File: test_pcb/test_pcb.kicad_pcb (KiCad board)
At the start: 2 copper layers, 62.2 x 43.2 mm, 19 parts, among them K0 KEYSW, K1 KEYSW, K2 KEYSW, K3 KEYSW, K5 KEYSW, U1 74HC595, U2 Teensy3.2

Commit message: updated test_pcb
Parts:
- added LVC9_HOLES: LVC9 Attach, cherry_rgb:LVC9_HOLES, F.Cu at (200.0, 94.0)
- added P1: CONN_01X08, Pin_Headers:Pin_Header_Straight_1x08_Pitch2.00mm, F.Cu at (230.0, 78.5)
- added P2: CONN_01X08, Pin_Headers:Pin_Header_Straight_1x08_Pitch2.00mm, F.Cu at (170.0, 92.5)
- added U0: Teensy3.2, Teensy:Teensy30_31_32_LC, F.Cu at (248.0, 90.5)
- U1: footprint SMD_Packages:SO-16-L -> Housings_SSOP:TSSOP-16_4.4x5mm_Pitch0.65mm
- U2: value Teensy3.2 -> 74HC595; footprint Socket_Strips:Socket_Strip_Angled_2x27_Pitch2.54mm -> Housings_SSOP:TSSOP-16_4.4x5mm_Pitch0.65mm; moved to B.Cu
- moved U2 36.3 mm to (223.5, 89.0), turned to 0 degrees
- moved R1 10.6 mm to (215.0, 88.5)
- moved R2 10.6 mm to (224.5, 107.5)
- moved U1 5.64 mm to (223.5, 81.5), turned to 0 degrees
- moved D1 2.07 mm to (174.5, 98.0)
- moved D3 2.03 mm to (193.5, 98.0)
- moved D0 2.02 mm to (184.0, 79.0)
- moved D5 1.99 mm to (212.5, 98.0)
- moved D2 1.98 mm to (203.0, 79.0)
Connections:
- D3 pad 1: Net-(D3-Pad1) -> row1
- U1 pad 1: row1_sled_g -> col0_sled_cath
- U1 pad 11: Net-(U1-Pad11) -> sr_clk0
- U1 pad 13: Net-(U1-Pad13) -> GND
- U1 pad 14: sr_data -> sr_data0
- U1 pad 15: row1_sled_b -> col1_sled_cath
- U1 pad 2: row1_sled_r -> col2_sled_cath
- U1 pad 3: row0_sled_b -> Net-(U1-Pad3)
- U1 pad 4: row0_sled_g -> Net-(U1-Pad4)
- U1 pad 5: row0_sled_r -> Net-(U1-Pad5)
- U1 pad 6: col1_sled_cath -> Net-(U1-Pad6)
- U1 pad 7: col0_sled_cath -> Net-(U1-Pad7)
- U2 pad 1: Net-(U2-Pad1) -> row1_sled_g
- U2 pad 11: Net-(U2-Pad11) -> sr_clk0
- U2 pad 13: Net-(U2-Pad13) -> GND
- U2 pad 14: Net-(U2-Pad14) -> sr_data1
- U2 pad 15: Net-(U2-Pad15) -> row1_sled_b
- U2 pad 16: Net-(U2-Pad16) -> VCC
- U2 pad 2: row0 -> row1_sled_r
- U2 pad 3: row1 -> row0_sled_b
- U2 pad 4: col0 -> row0_sled_g
- U2 pad 5: col1 -> row0_sled_r
- U2 pad 6: sr_data -> Net-(U2-Pad6)
- U2 pad 7: col2_sled_cath -> Net-(U2-Pad7)
- U2 pad 8: Net-(U2-Pad8) -> GND

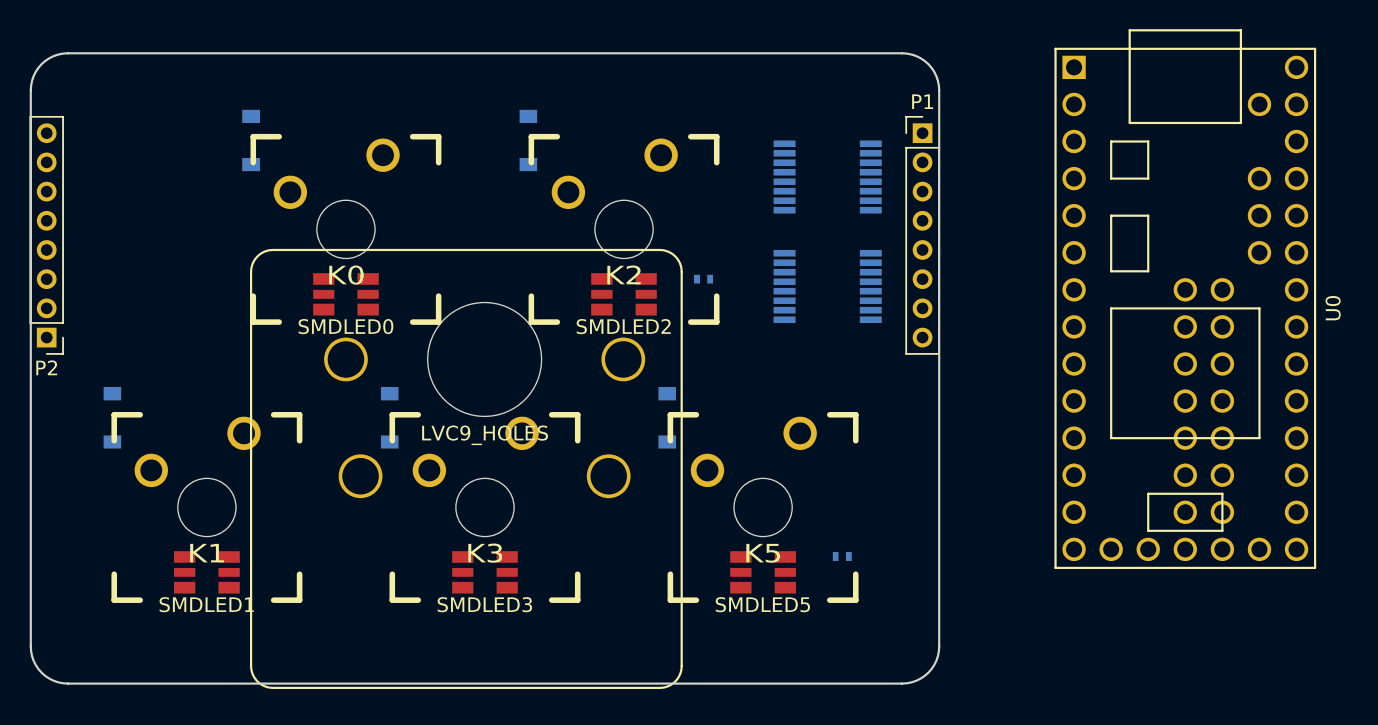
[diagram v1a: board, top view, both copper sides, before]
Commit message: test_pcb first pass complete
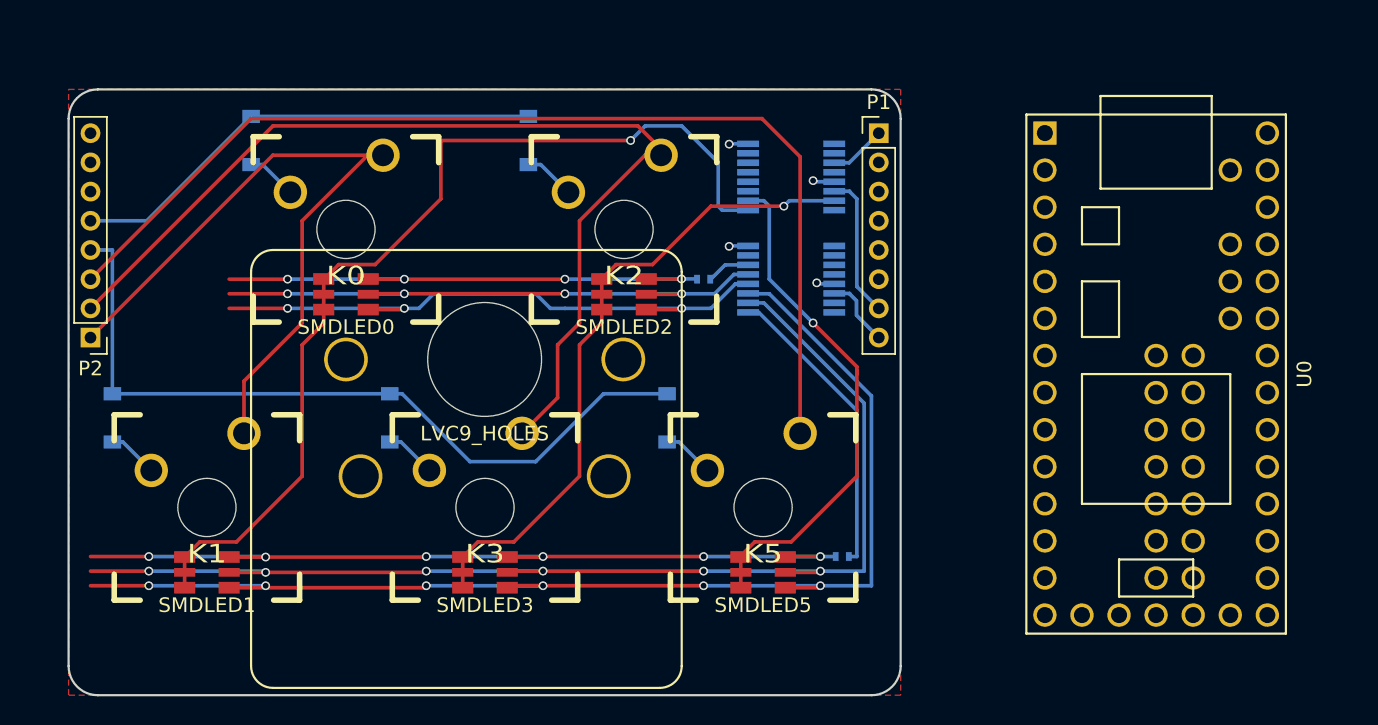
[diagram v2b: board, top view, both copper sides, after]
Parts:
- moved U0 4.92 mm to (246.0, 95.0)
- moved P1 3.00 mm to (227.0, 78.5)
- moved P2 3.00 mm to (173.0, 92.5)
- moved U2 2.55 mm to (221.0, 88.5)
- moved U1 2.50 mm to (221.0, 81.5)
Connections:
- U2 pad 1: row1_sled_g -> row1_sled_r
- U2 pad 15: row1_sled_b -> Net-(U2-Pad15)
- U2 pad 2: row1_sled_r -> row1_sled_g
- U2 pad 3: row0_sled_b -> row1_sled_b
- U2 pad 4: row0_sled_g -> row0_sled_b
- U2 pad 5: row0_sled_r -> row0_sled_g
- U2 pad 6: Net-(U2-Pad6) -> row0_sled_r
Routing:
- net row1_sled_b: track 0.00 -> 85.5 mm, vias 0 -> 6
- net row1_sled_g: track 0.00 -> 82.8 mm, vias 0 -> 6
- net col2: track 0.00 -> 73.2 mm
- net col1: track 0.00 -> 69.0 mm, vias 0 -> 1
- net col0_sled_cath: track 0.00 -> 66.5 mm, vias 0 -> 1
- net Net-(R2-Pad2): track 0.00 -> 58.5 mm, vias 0 -> 6
- net row1: track 0.00 -> 53.2 mm
- net col0: track 0.00 -> 48.8 mm
- net col1_sled_cath: track 0.00 -> 45.0 mm, vias 0 -> 1
- net row0_sled_b: track 0.00 -> 42.0 mm, vias 0 -> 3
- net row0_sled_g: track 0.00 -> 41.0 mm, vias 0 -> 4
- net Net-(R1-Pad2): track 0.00 -> 37.0 mm, vias 0 -> 4
- net col2_sled_cath: track 0.00 -> 35.2 mm, vias 0 -> 1
- net row0: track 0.00 -> 33.0 mm
- net row1_sled_r: track 0.00 -> 20.8 mm
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- added copper zone on F.Cu, net GND
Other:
- board size 62.2 x 43.2 mm -> 57 x 41.5 mm

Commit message: test_pcb small stuff
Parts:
- added P0: CONN_01X08, Connectors_Molex:Molex_PicoBlade_53261-0871_08x1.25mm_Angled, F.Cu at (197.8, 124.5)
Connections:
- P1 pad 5: Net-(P1-Pad5) -> VCC
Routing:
- net VCC: track 0.00 -> 13.1 mm, vias 0 -> 2

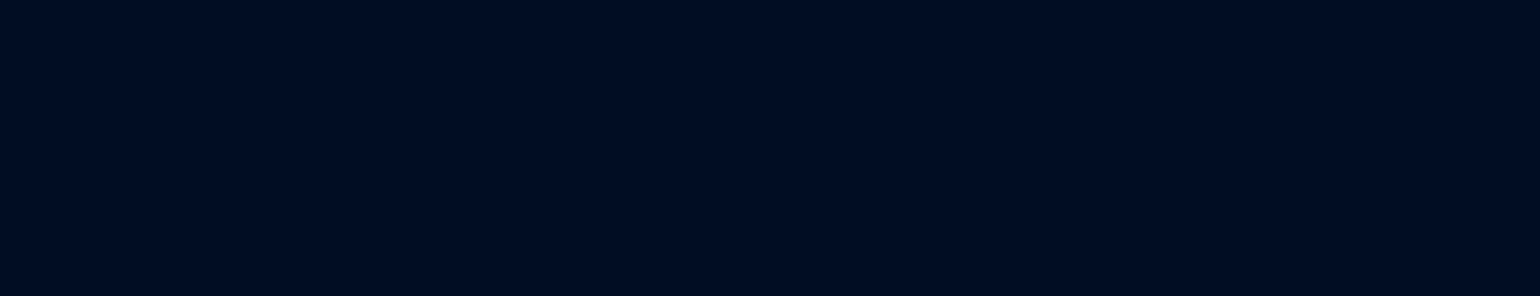
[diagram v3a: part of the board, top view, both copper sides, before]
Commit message: test experiment with 11/12ths keys
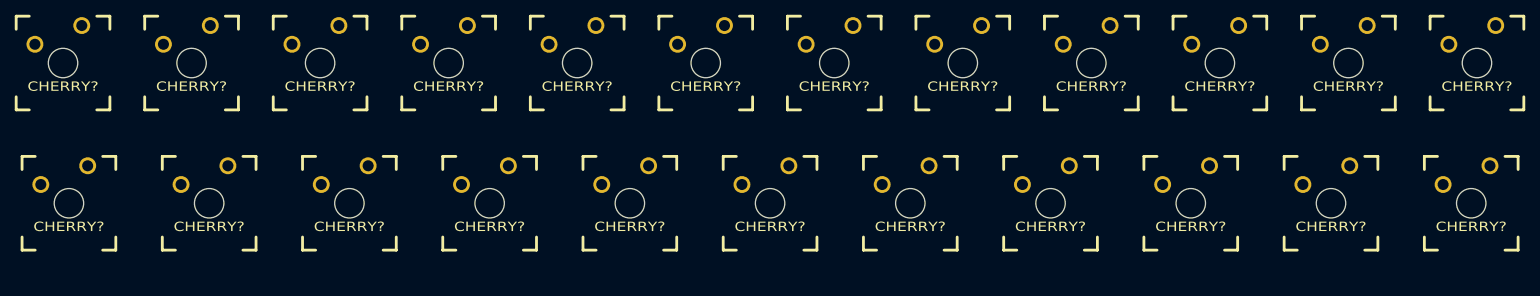
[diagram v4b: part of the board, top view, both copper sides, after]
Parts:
- added CHERRY?: MX, cherry_rgb:CHERRY_PLATE_91.6H, F.Cu at (250.8, 23.0)
- added CHERRY?: MX, cherry_rgb:CHERRY_PLATE_91.6H, F.Cu at (94.0, 23.0)
- added CHERRY?: MX, cherry_rgb:CHERRY_PLATE_91.6H, F.Cu at (76.6, 23.0)
- added CHERRY?: MX, cherry_rgb:CHERRY_PLATE_NH_100H, F.Cu at (250.0, 42.0)
- added CHERRY?: MX, cherry_rgb:CHERRY_PLATE_NH_100H, F.Cu at (60.0, 42.0)
- added CHERRY?: MX, cherry_rgb:CHERRY_PLATE_NH_100H, F.Cu at (231.0, 42.0)
- added CHERRY?: MX, cherry_rgb:CHERRY_PLATE_NH_100H, F.Cu at (79.0, 42.0)
- added CHERRY?: MX, cherry_rgb:CHERRY_PLATE_NH_100H, F.Cu at (98.0, 42.0)
- added CHERRY?: MX, cherry_rgb:CHERRY_PLATE_NH_100H, F.Cu at (212.0, 42.0)
- added CHERRY?: MX, cherry_rgb:CHERRY_PLATE_NH_100H, F.Cu at (193.0, 42.0)
- added CHERRY?: MX, cherry_rgb:CHERRY_PLATE_NH_100H, F.Cu at (174.0, 42.0)
- added CHERRY?: MX, cherry_rgb:CHERRY_PLATE_91.6H, F.Cu at (233.4, 23.0)
- added CHERRY?: MX, cherry_rgb:CHERRY_PLATE_NH_100H, F.Cu at (155.0, 42.0)
- added CHERRY?: MX, cherry_rgb:CHERRY_PLATE_NH_100H, F.Cu at (136.0, 42.0)
- added CHERRY?: MX, cherry_rgb:CHERRY_PLATE_NH_100H, F.Cu at (117.0, 42.0)
- added CHERRY?: MX, cherry_rgb:CHERRY_PLATE_91.6H, F.Cu at (59.2, 23.0)
- added CHERRY?: MX, cherry_rgb:CHERRY_PLATE_91.6H, F.Cu at (215.9, 23.0)
- added CHERRY?: MX, cherry_rgb:CHERRY_PLATE_91.6H, F.Cu at (198.5, 23.0)
- added CHERRY?: MX, cherry_rgb:CHERRY_PLATE_91.6H, F.Cu at (181.1, 23.0)
- added CHERRY?: MX, cherry_rgb:CHERRY_PLATE_91.6H, F.Cu at (163.7, 23.0)
- added CHERRY?: MX, cherry_rgb:CHERRY_PLATE_91.6H, F.Cu at (146.3, 23.0)
- added CHERRY?: MX, cherry_rgb:CHERRY_PLATE_91.6H, F.Cu at (128.9, 23.0)
- added CHERRY?: MX, cherry_rgb:CHERRY_PLATE_91.6H, F.Cu at (111.4, 23.0)

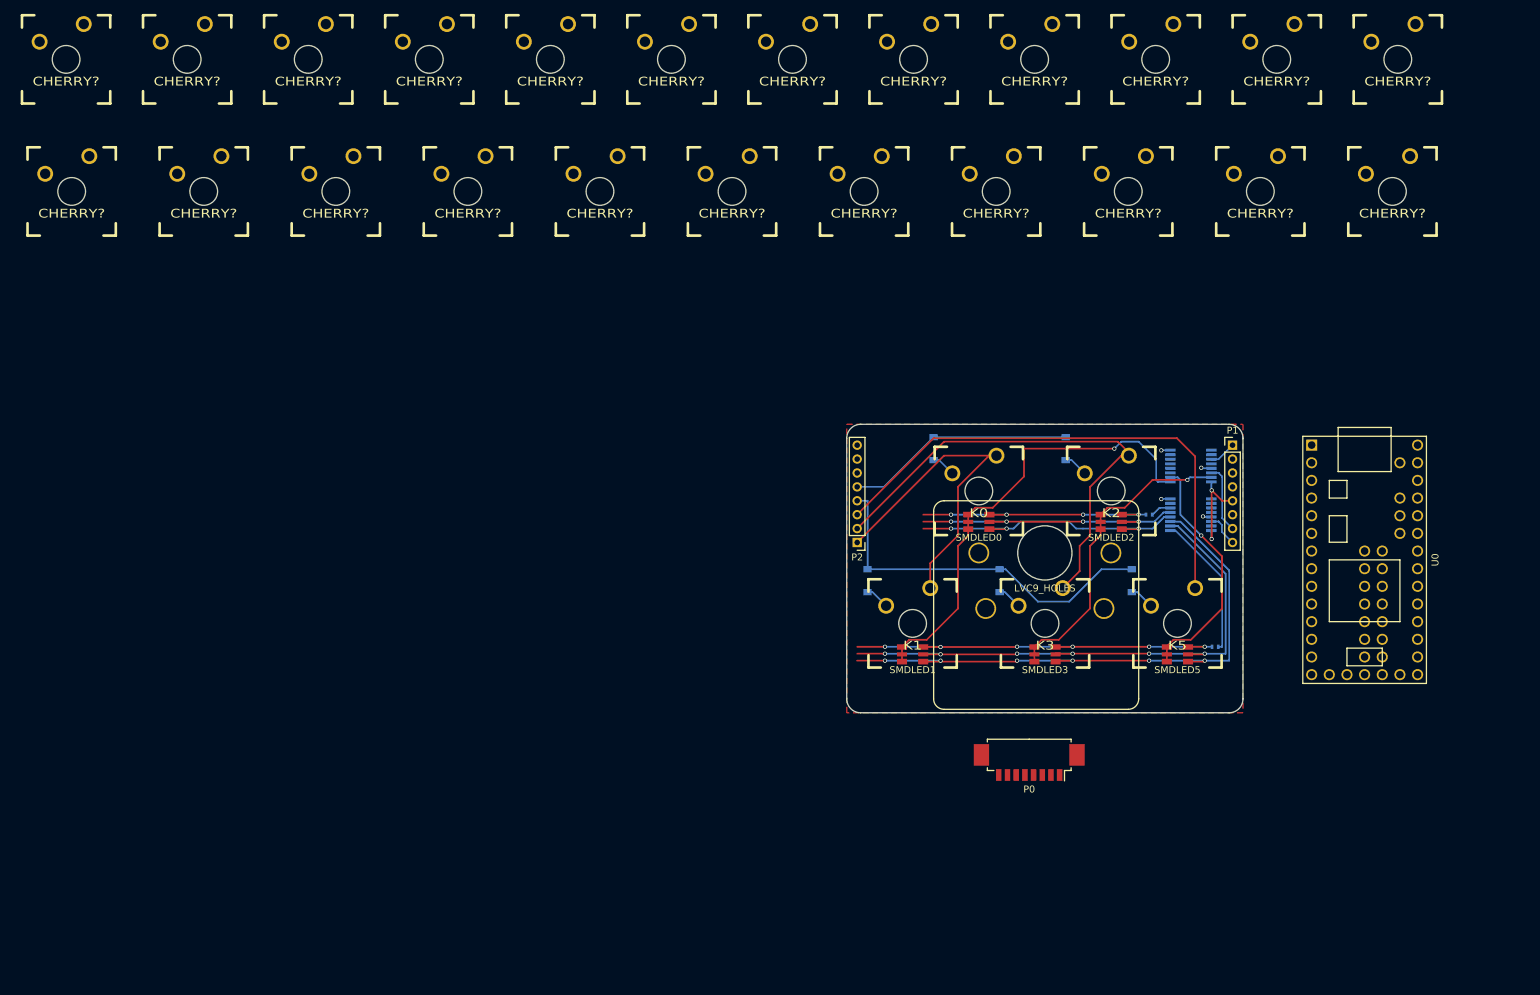
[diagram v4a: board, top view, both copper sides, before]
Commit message: test is now a numpad for led testing + a 6 key test for the trackpoint
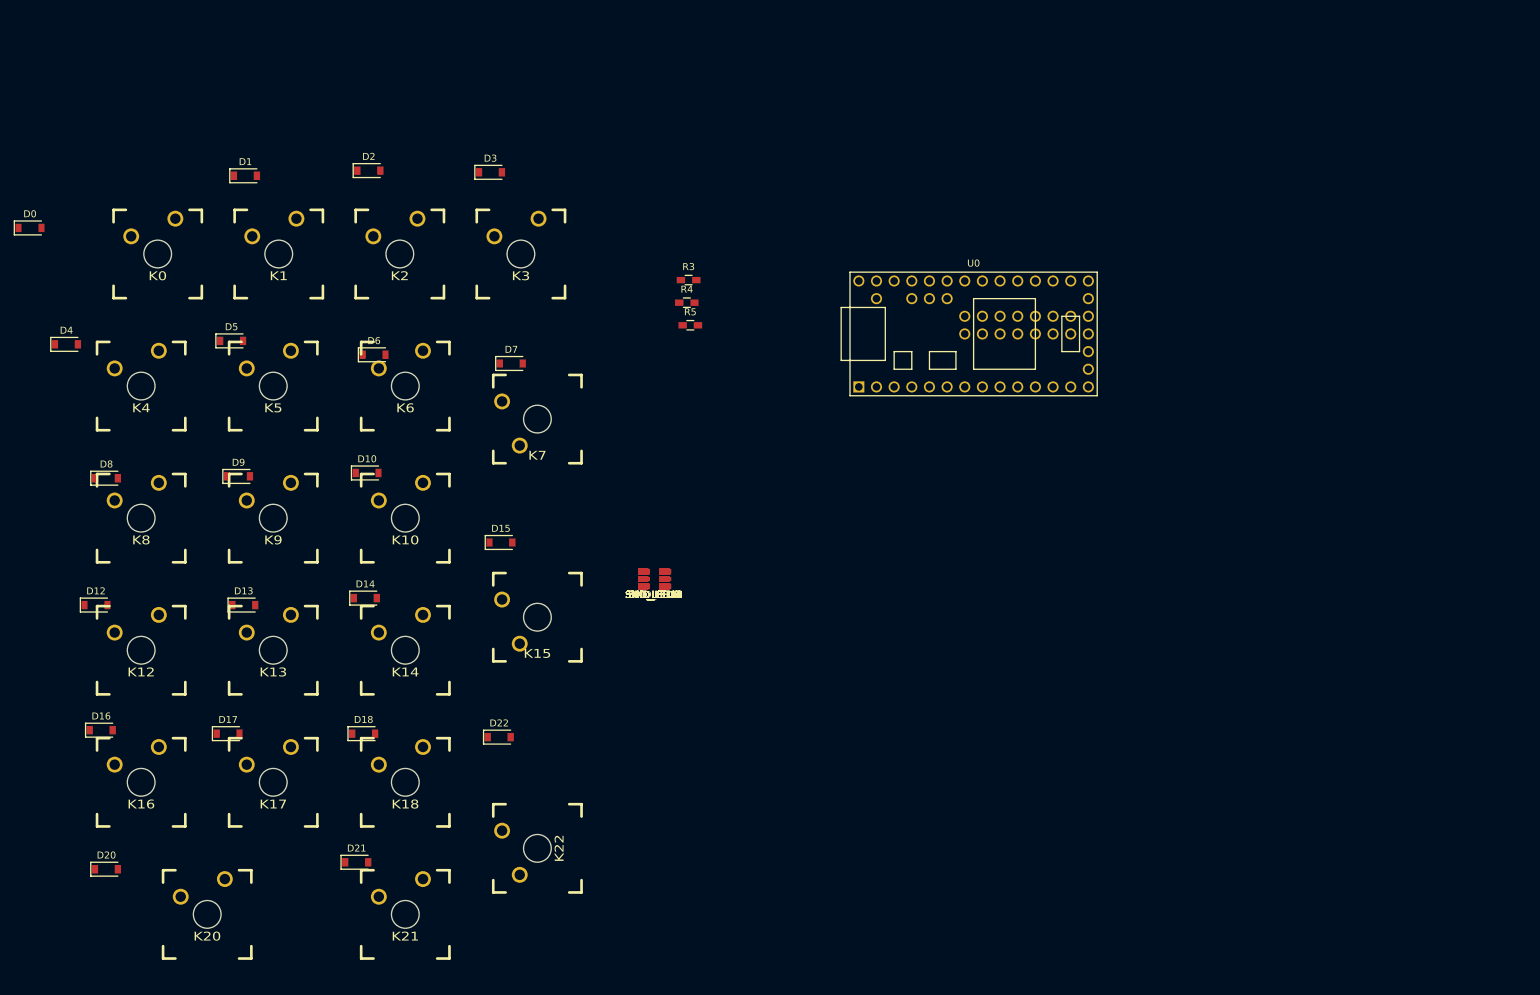
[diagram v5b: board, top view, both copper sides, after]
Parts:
- removed CHERRY? (x12): MX, cherry_rgb:CHERRY_PLATE_91.6H
- removed CHERRY? (x11): MX, cherry_rgb:CHERRY_PLATE_NH_100H
- removed LVC9_HOLES: LVC9 Attach, cherry_rgb:LVC9_HOLES
- removed P0: CONN_01X08, Connectors_Molex:Molex_PicoBlade_53261-0871_08x1.25mm_Angled
- removed P1, P2: CONN_01X08, Pin_Headers:Pin_Header_Straight_1x08_Pitch2.00mm
- removed R1, R2: R, Resistors_SMD:R_0402
- removed SMDLED0, SMDLED1, SMDLED2, SMDLED3, SMDLED5: LED_RGB, cherry_rgb:SMLVN6RGB
- removed U1, U2: 74HC595, Housings_SSOP:TSSOP-16_4.4x5mm_Pitch0.65mm
- added D10: D, Diodes_SMD:D_SOD-123, F.Cu at (102.5, 82.5)
- added D12: D, Diodes_SMD:D_SOD-123, F.Cu at (63.5, 101.5)
- added D13: D, Diodes_SMD:D_SOD-123, F.Cu at (84.8, 101.5)
- added D14: D, Diodes_SMD:D_SOD-123, F.Cu at (102.2, 100.5)
- added D15: D, Diodes_SMD:D_SOD-123, F.Cu at (121.8, 92.5)
- added D16: D, Diodes_SMD:D_SOD-123, F.Cu at (64.2, 119.5)
- added D17: D, Diodes_SMD:D_SOD-123, F.Cu at (82.5, 120.0)
- added D18: D, Diodes_SMD:D_SOD-123, F.Cu at (102.0, 120.0)
- added D20: D, Diodes_SMD:D_SOD-123, F.Cu at (65.0, 139.5)
- added D21: D, Diodes_SMD:D_SOD-123, F.Cu at (101.0, 138.5)
- added D22: D, Diodes_SMD:D_SOD-123, F.Cu at (121.5, 120.5)
- added D4: D, Diodes_SMD:D_SOD-123, F.Cu at (59.2, 64.0)
- added D6: D, Diodes_SMD:D_SOD-123, F.Cu at (103.5, 65.5)
- added D7: D, Diodes_SMD:D_SOD-123, F.Cu at (123.2, 66.8)
- added D8: D, Diodes_SMD:D_SOD-123, F.Cu at (65.0, 83.2)
- added D9: D, Diodes_SMD:D_SOD-123, F.Cu at (84.0, 83.0)
- added K10: KEYSW, cherry_rgb:CHERRY_PLATE_NH_100H, F.Cu at (108.0, 89.0)
- added K12: KEYSW, cherry_rgb:CHERRY_PLATE_NH_100H, F.Cu at (70.0, 108.0)
- added K13: KEYSW, cherry_rgb:CHERRY_PLATE_NH_100H, F.Cu at (89.0, 108.0)
- added K14: KEYSW, cherry_rgb:CHERRY_PLATE_NH_100H, F.Cu at (108.0, 108.0)
- added K15: KEYSW, cherry_rgb:CHERRY_PLATE_150V, F.Cu at (127.0, 103.2)
- added K16: KEYSW, cherry_rgb:CHERRY_PLATE_NH_100H, F.Cu at (70.0, 127.0)
- added K17: KEYSW, cherry_rgb:CHERRY_PLATE_NH_100H, F.Cu at (89.0, 127.0)
- added K18: KEYSW, cherry_rgb:CHERRY_PLATE_NH_100H, F.Cu at (108.0, 127.0)
- added K20: KEYSW, cherry_rgb:CHERRY_PLATE_200H, F.Cu at (79.5, 146.0)
- added K21: KEYSW, cherry_rgb:CHERRY_PLATE_NH_100H, F.Cu at (108.0, 146.0)
- added K22: KEYSW, cherry_rgb:CHERRY_PLATE_200V, F.Cu at (127.0, 136.5)
- added K4: KEYSW, cherry_rgb:CHERRY_PLATE_NH_100H, F.Cu at (70.0, 70.0)
- added K6: KEYSW, cherry_rgb:CHERRY_PLATE_NH_100H, F.Cu at (108.0, 70.0)
- added K7: KEYSW, cherry_rgb:CHERRY_PLATE_150V, F.Cu at (127.0, 74.8)
- added K8: KEYSW, cherry_rgb:CHERRY_PLATE_NH_100H, F.Cu at (70.0, 89.0)
- added K9: KEYSW, cherry_rgb:CHERRY_PLATE_NH_100H, F.Cu at (89.0, 89.0)
- added R3: R, Resistors_SMD:R_0603_HandSoldering, F.Cu at (148.8, 54.8)
- added R4: R, Resistors_SMD:R_0603_HandSoldering, F.Cu at (148.5, 58.0)
- added R5: R, Resistors_SMD:R_0603_HandSoldering, F.Cu at (149.0, 61.2)
- added SMD_LED1: SMLVN6RGB, cherry_rgb:SMLVN6RGB, F.Cu at (144.0, 97.8)
- added SMD_LED10, SMD_LED11, SMD_LED12, SMD_LED13, SMD_LED14, SMD_LED15, SMD_LED16, SMD_LED17, SMD_LED18, SMD_LED19, SMD_LED2, SMD_LED20, SMD_LED21, SMD_LED3, SMD_LED4, SMD_LED5, SMD_LED6, SMD_LED7, SMD_LED8, SMD_LED9: SMLVN6RGB, cherry_rgb:SMLVN6RGB, F.Cu at (143.8, 97.8)
- D0, D1, D2, D3, D5: moved to F.Cu
- K0, K1, K2, K3: footprint cherry_rgb:CHERRY_PLATE_NH_100H -> cherry_rgb:CHERRY_PLATE_91.6H
- moved K5 134.5 mm to (89.0, 70.0)
- moved D5 134.0 mm to (83.0, 63.5), turned to 0 degrees
- moved D0 133.8 mm to (54.0, 47.2), turned to 0 degrees
- moved K0 122.9 mm to (72.4, 51.0)
- moved D2 107.9 mm to (102.8, 39.0), turned to 0 degrees
- moved K2 107.9 mm to (107.2, 51.0)
- moved D1 106.8 mm to (85.0, 39.8), turned to 0 degrees
- moved K1 105.5 mm to (89.8, 51.0)
- moved D3 93.9 mm to (120.2, 39.2), turned to 0 degrees
- moved K3 92.2 mm to (124.6, 51.0)
- moved U0 65.0 mm to (189.8, 62.5), turned to 0 degrees
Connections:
- D0 pad 1: row0 -> Net-(D0-Pad1)
- D1 pad 1: row1 -> Net-(D1-Pad1)
- D2 pad 1: row0 -> Net-(D2-Pad1)
- D3 pad 1: row1 -> Net-(D3-Pad1)
- D5 pad 1: row1 -> Net-(D5-Pad1)
- K0 pad 1: col0 -> r0
- K1 pad 1: col0 -> r0
- K2 pad 1: col1 -> r0
- K3 pad 1: col1 -> r0
- K5 pad 1: col2 -> r1
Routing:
- net row1_sled_b: track 85.5 -> 0.00 mm, vias 6 -> 0
- net row1_sled_g: track 82.8 -> 0.00 mm, vias 6 -> 0
- net col2: track 73.2 -> 0.00 mm
- net col1: track 69.0 -> 0.00 mm, vias 1 -> 0
- net col0_sled_cath: track 66.5 -> 0.00 mm, vias 1 -> 0
- net Net-(R2-Pad2): track 58.5 -> 0.00 mm, vias 6 -> 0
- net row1: track 53.2 -> 0.00 mm
- net col0: track 48.8 -> 0.00 mm
- net col1_sled_cath: track 45.0 -> 0.00 mm, vias 1 -> 0
- net row0_sled_b: track 42.0 -> 0.00 mm, vias 3 -> 0
- net row0_sled_g: track 41.0 -> 0.00 mm, vias 4 -> 0
- net Net-(R1-Pad2): track 37.0 -> 0.00 mm, vias 4 -> 0
- net col2_sled_cath: track 35.2 -> 0.00 mm, vias 1 -> 0
- net row0: track 33.0 -> 0.00 mm
- net row1_sled_r: track 20.8 -> 0.00 mm
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- removed copper zone on F.Cu, net GND
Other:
- board outline removed
